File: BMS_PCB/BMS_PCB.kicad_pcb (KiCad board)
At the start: 2 copper layers, 165 parts, among them IC1 TPS560430XFDBVT, IC3 AMC1350DWVR, IC4 AMC1350DWVR, IC5 AMC1350DWVR, IC6 AMC1350DWVR, J1 Conn_01x37, J2 Conn_01x15, K1 J1021AS35VDC.20, Q1 2N7002KT7G, U1 TLV2404IDR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

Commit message: Footprints
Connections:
- J1 pad 2: Relais_in+ -> Current
- J1 pad 4: Relais_out+ -> Relais_in+
- J1 pad 6: Current -> Relais_out+
- K1 pad 1: (no net) -> Net-(K1-Pad1)
- K1 pad 6: Net-(K1-Pad1) -> unconnected-(K1-Pad6)
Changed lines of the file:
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@@
 			(psa4output no)
 			(plot_black_and_white yes)
+			(plotinvisibletext no)
 			(sketchpadsonfab no)
 			(plotpadnumbers no)
@@
 	(net 192 "Net-(J1-Pin_15)")
 	(net 193 "Net-(J1-Pin_14)")
+	(net 194 "unconnected-(K1-Pad6)")
 	(footprint "Resistor_SMD:R_0603_1608Metric_Pad0.98x0.95mm_HandSolder"
 		(layer "F.Cu")
@@
 			(layers "*.Cu" "*.Mask")
 			(remove_unused_layers no)
-			(net 20 "Relais_in+")
+			(net 59 "Current")
 			(pinfunction "Pin_2")
 			(pintype "passive")
@@
 			(layers "*.Cu" "*.Mask")
 			(remove_unused_layers no)
-			(net 65 "Relais_out+")
+			(net 20 "Relais_in+")
 			(pinfunction "Pin_4")
 			(pintype "passive")
@@
 			(layers "*.Cu" "*.Mask")
 			(remove_unused_layers no)
-			(net 59 "Current")
+			(net 65 "Relais_out+")
 			(pinfunction "Pin_6")
 			(pintype "passive")
@@
 			(layers "*.Cu" "*.Mask")
 			(remove_unused_layers no)
+			(net 186 "Net-(K1-Pad1)")
 			(pinfunction "1")
 			(pintype "passive")
@@
 			(layers "*.Cu" "*.Mask")
 			(remove_unused_layers no)
-			(net 186 "Net-(K1-Pad1)")
+			(net 194 "unconnected-(K1-Pad6)")
 			(pinfunction "6")
 			(pintype "passive+no_connect")

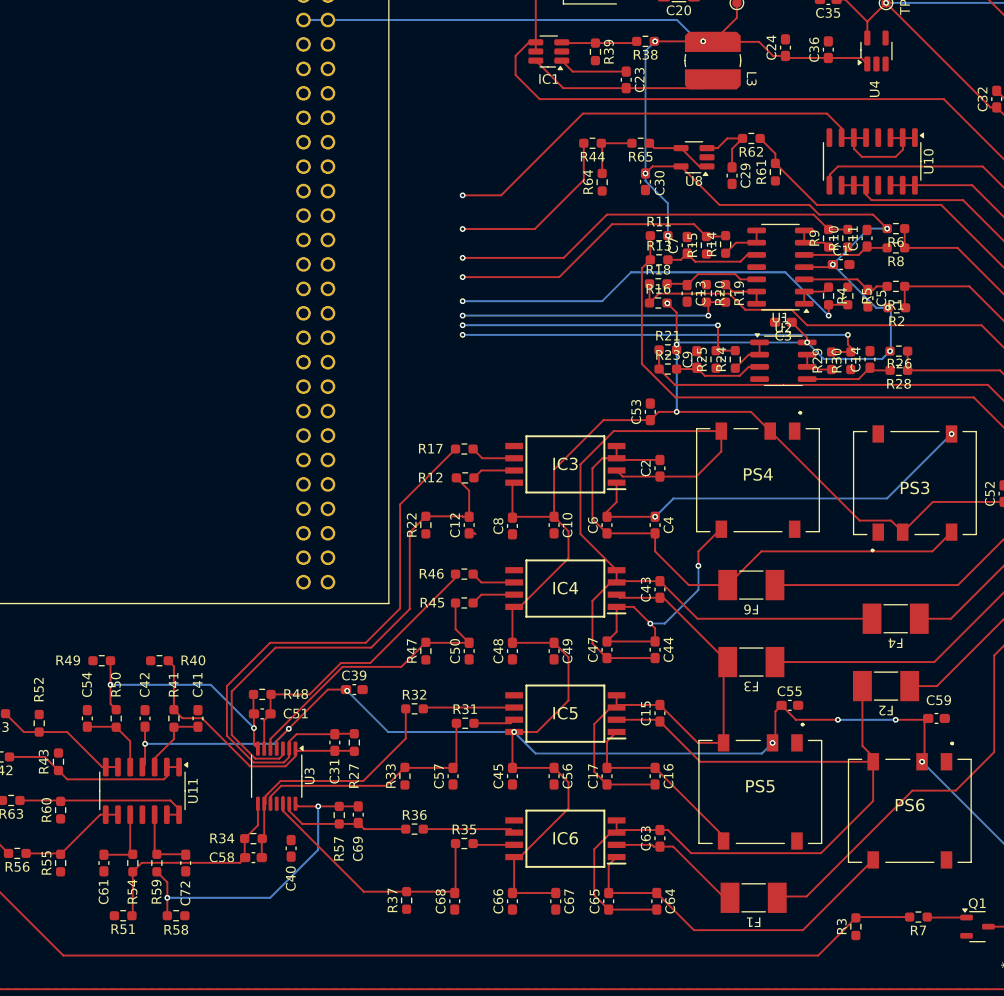
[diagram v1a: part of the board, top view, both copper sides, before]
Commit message: kleine Änderungen
Grounding angepasst
Connector angepasst
Beschriftung angepasst
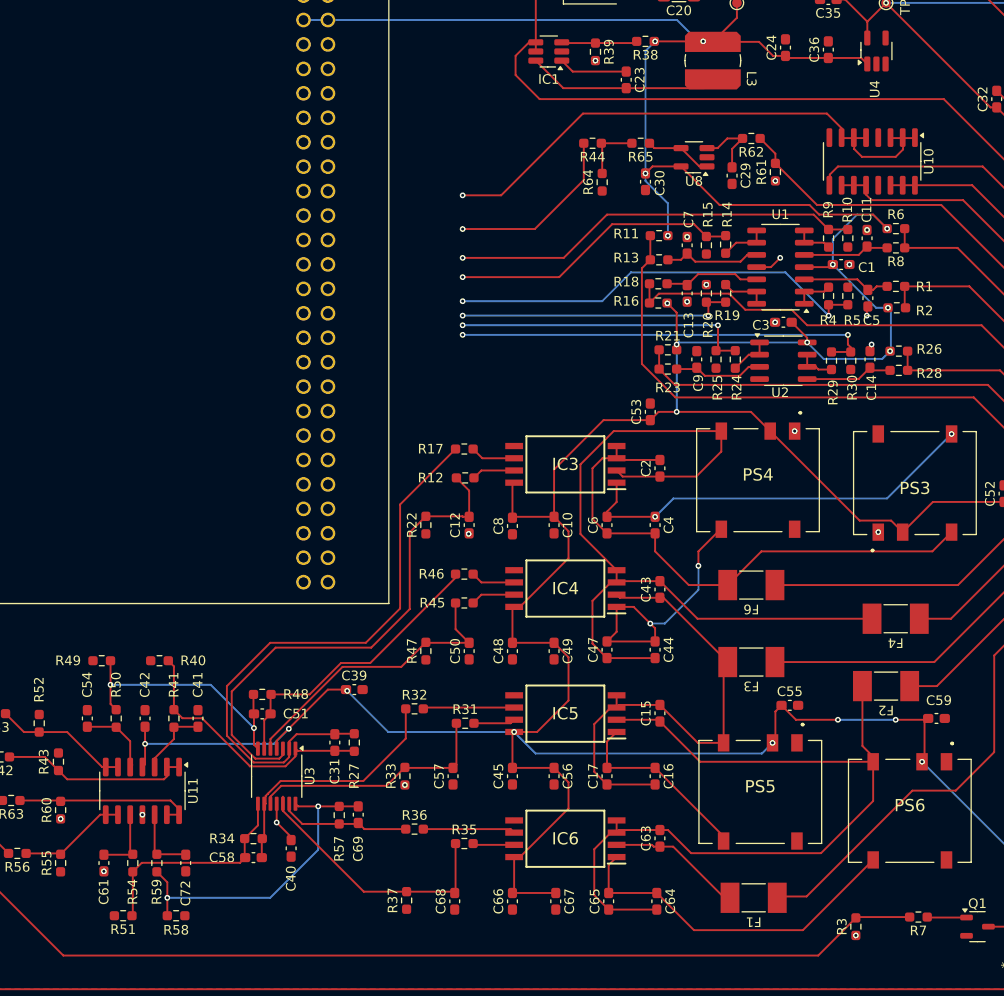
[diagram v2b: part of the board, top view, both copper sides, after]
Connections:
- J1 pad 2: Current -> Relais_in+
- J1 pad 4: Relais_in+ -> Relais_out-
- J1 pad 5: Relais_out- -> Relais_out+
- J1 pad 6: Relais_out+ -> Current
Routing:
- net GND: track 16.8 -> 24.0 mm, vias 0 -> 20
- net +5V: track 456.8 -> 459.6 mm

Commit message: Bugfixes
noch ein paar Fehler ausgemerzt
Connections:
- J1 pad 4: Relais_out- -> Relais_out+
- J1 pad 5: Relais_out+ -> Relais_out-
- K1 pad 6: unconnected-(K1-Pad6) -> Net-(K1-Pad6)
- R_Precharge1 pad 2: Net-(K1-Pad1) -> Net-(K1-Pad6)
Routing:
- net +BATT: track 118.2 -> 104.5 mm
- net Net-(K1-Pad6): track 0.00 -> 6.92 mm
- net Net-(K1-Pad1): track 6.92 -> 0.00 mm
- net +5V: vias 20 -> 19
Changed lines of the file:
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@@
 	(net 192 "Net-(J1-Pin_15)")
 	(net 193 "Net-(J1-Pin_14)")
-	(net 194 "unconnected-(K1-Pad6)")
+	(net 194 "Net-(K1-Pad6)")
 	(footprint "Resistor_SMD:R_0603_1608Metric_Pad0.98x0.95mm_HandSolder"
 		(layer "F.Cu")
@@
 			(layers "*.Cu" "*.Mask")
 			(remove_unused_layers no)
-			(net 57 "Relais_out-")
+			(net 65 "Relais_out+")
 			(pinfunction "Pin_4")
 			(pintype "passive")
@@
 			(layers "*.Cu" "*.Mask")
 			(remove_unused_layers no)
-			(net 65 "Relais_out+")
+			(net 57 "Relais_out-")
 			(pinfunction "Pin_5")
 			(pintype "passive")
@@
 			(layers "*.Cu" "*.Mask")
 			(remove_unused_layers no)
-			(net 194 "unconnected-(K1-Pad6)")
+			(net 194 "Net-(K1-Pad6)")
 			(pinfunction "6")
 			(pintype "passive+no_connect")
@@
 			(layers "F.Cu" "F.Mask" "F.Paste")
 			(roundrect_rratio 0.078125)
-			(net 186 "Net-(K1-Pad1)")
+			(net 194 "Net-(K1-Pad6)")
 			(pintype "passive")
 		)
@@
 	)
 	(via
-		(at 211.275625 88.724375)
-		(size 0.6)
-		(drill 0.3)
-		(layers "F.Cu" "B.Cu")
-		(net 1)
-	)
-	(via
 		(at 195.35 133.2675)
 		(size 0.6)
@@
 	)
 	(segment
-		(start 244.5 49.316225)
-		(end 264 68.816225)
-		(width 0.2)
-		(layer "F.Cu")
-		(net 16)
-	)
-	(segment
-		(start 253.5 118.51)
-		(end 256.49 118.51)
+		(start 241.4775 40.9225)
+		(end 244.5 43.945)
 		(width 0.2)
 		(layer "F.Cu")
@@
 	(segment
 		(start 264 68.816225)
-		(end 264 111)
+		(end 264 110.5)
 		(width 0.2)
 		(layer "F.Cu")
@@
 	)
 	(segment
-		(start 241.4775 40.9225)
-		(end 244.5 43.945)
+		(start 255.99 118.51)
+		(end 253.5 118.51)
 		(width 0.2)
 		(layer "F.Cu")
@@
 	)
 	(segment
-		(start 244.5 43.945)
-		(end 244.5 49.316225)
+		(start 238.4775 40.9225)
+		(end 238.4775 39.145)
 		(width 0.2)
 		(layer "F.Cu")
@@
 	)
 	(segment
-		(start 256.49 118.51)
-		(end 264 111)
+		(start 244.5 43.945)
+		(end 244.5 49.316225)
 		(width 0.2)
 		(layer "F.Cu")
@@
 	)
 	(segment
-		(start 238.4775 40.9225)
-		(end 238.4775 39.145)
+		(start 241.4775 40.9225)
+		(end 238.4775 40.9225)
 		(width 0.2)
 		(layer "F.Cu")
@@
 	)
 	(segment
-		(start 264 111)
-		(end 264 97.5)
+		(start 264 110.5)
+		(end 255.99 118.51)
 		(width 0.2)
 		(layer "F.Cu")
@@
 	)
 	(segment
-		(start 241.4775 40.9225)
-		(end 238.4775 40.9225)
+		(start 244.5 49.316225)
+		(end 264 68.816225)
 		(width 0.2)
 		(layer "F.Cu")
@@
 	)
 	(segment
-		(start 242.95 76.45)
-		(end 250.385 83.885)
+		(start 237 76.45)
+		(end 243.225 76.45)
 		(width 0.2)
 		(layer "F.Cu")
@@
 	)
 	(segment
-		(start 237 76.45)
-		(end 242.95 76.45)
+		(start 250.385 83.885)
+		(end 250.66 83.885)
 		(width 0.2)
 		(layer "F.Cu")
@@
 	)
 	(segment
-		(start 250.385 83.885)
+		(start 243.225 76.45)
 		(end 250.66 83.885)
 		(width 0.2)
@@
 	)
 	(segment
-		(start 252.9 145.42045)
-		(end 251.84 146.48045)
-		(width 0.2)
-		(layer "F.Cu")
-		(net 186)
-	)
-	(segment
-		(start 252.9 140)
-		(end 252.9 145.42045)
-		(width 0.2)
-		(layer "F.Cu")
-		(net 186)
-	)
-	(segment
 		(start 204.5 75.225)
 		(end 204.5 72.175)
@@
 		(net 193)
 	)
+	(segment
+		(start 252.9 145.42045)
+		(end 251.84 146.48045)
+		(width 0.2)
+		(layer "F.Cu")
+		(net 194)
+	)
+	(segment
+		(start 252.9 140)
+		(end 252.9 145.42045)
+		(width 0.2)
+		(layer "F.Cu")
+		(net 194)
+	)
 	(zone

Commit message: Mittwoch 30.04.
Quadratisch Praktisch Gut
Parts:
- moved U7 15.0 mm to (164.0, 68.3), turned to 180 degrees
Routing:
- net Precharge_uC: track 129.6 -> 128.8 mm

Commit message: Bohrungen platziert
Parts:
- added H1: MountingHole_3.6mm, MountingHole:MountingHole_3.7mm, F.Cu at (30.4, 176.5)
- added H2: MountingHole_3.6mm, MountingHole:MountingHole_3.7mm, F.Cu at (30.4, 92.5)
- added H3: MountingHole_3.6mm, MountingHole:MountingHole_3.7mm, F.Cu at (160.4, 176.5)
- moved D2 140.4 mm to (131.9, 173.4), turned to -90 degrees
- moved Q1 118.8 mm to (126.8, 175.4)
- moved R7 117.7 mm to (121.9, 175.4), turned to -90 degrees
- moved R3 115.6 mm to (117.4, 175.4), turned to -90 degrees
- moved K1 112.9 mm to (139.3, 163.2), turned to 0 degrees
- moved C1 111.9 mm to (119.2, 104.6)
- moved C12 111.9 mm to (80.6, 131.7)
- moved C13 111.9 mm to (103.2, 107.6)
- moved C14 111.9 mm to (122.2, 114.5)
- moved C3 111.9 mm to (113.2, 110.6)
- moved C45 111.9 mm to (85.1, 157.8)
- moved C48 111.9 mm to (85.1, 144.8)
- moved C5 111.9 mm to (122.0, 108.1)
- moved C50 111.9 mm to (80.6, 144.8)
- moved C59 111.9 mm to (129.1, 151.8)
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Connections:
- K1 pad 1: Net-(K1-Pad1) -> (no net)
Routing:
- net +5V: track 459.6 -> 486.5 mm, vias 19 -> 20
- net Temp3_uC: track 30.2 -> 12.4 mm
- net Temp2_uC: track 42.5 -> 25.7 mm
- net Temp1_uC: track 44.3 -> 28.0 mm
- net Current_uC: track 18.5 -> 3.59 mm
- net Temp5_uC: track 31.3 -> 16.8 mm
- net Temp4_uC: track 29.0 -> 14.9 mm
- net Temp6_uC: track 43.9 -> 30.1 mm
- net Net-(U3A-+): track 53.2 -> 41.2 mm
- net Vcc_Current: track 83.6 -> 95.2 mm
- net Net-(U3A--): track 62.3 -> 50.8 mm
- net Net-(PS1--VIN): track 38.3 -> 49.2 mm
- net Display_MOSI: track 61.6 -> 50.8 mm
- net -BATT: track 67.1 -> 56.3 mm
- net Touchdisplay_x-: track 65.0 -> 54.3 mm
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
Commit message: Bugfix
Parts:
- moved U7 0.39 mm to (58.6, 70.6)
